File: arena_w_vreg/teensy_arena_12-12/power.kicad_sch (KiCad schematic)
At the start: 2 parts, among them J1 Barrel_Jack, SW1 SW_SPDT

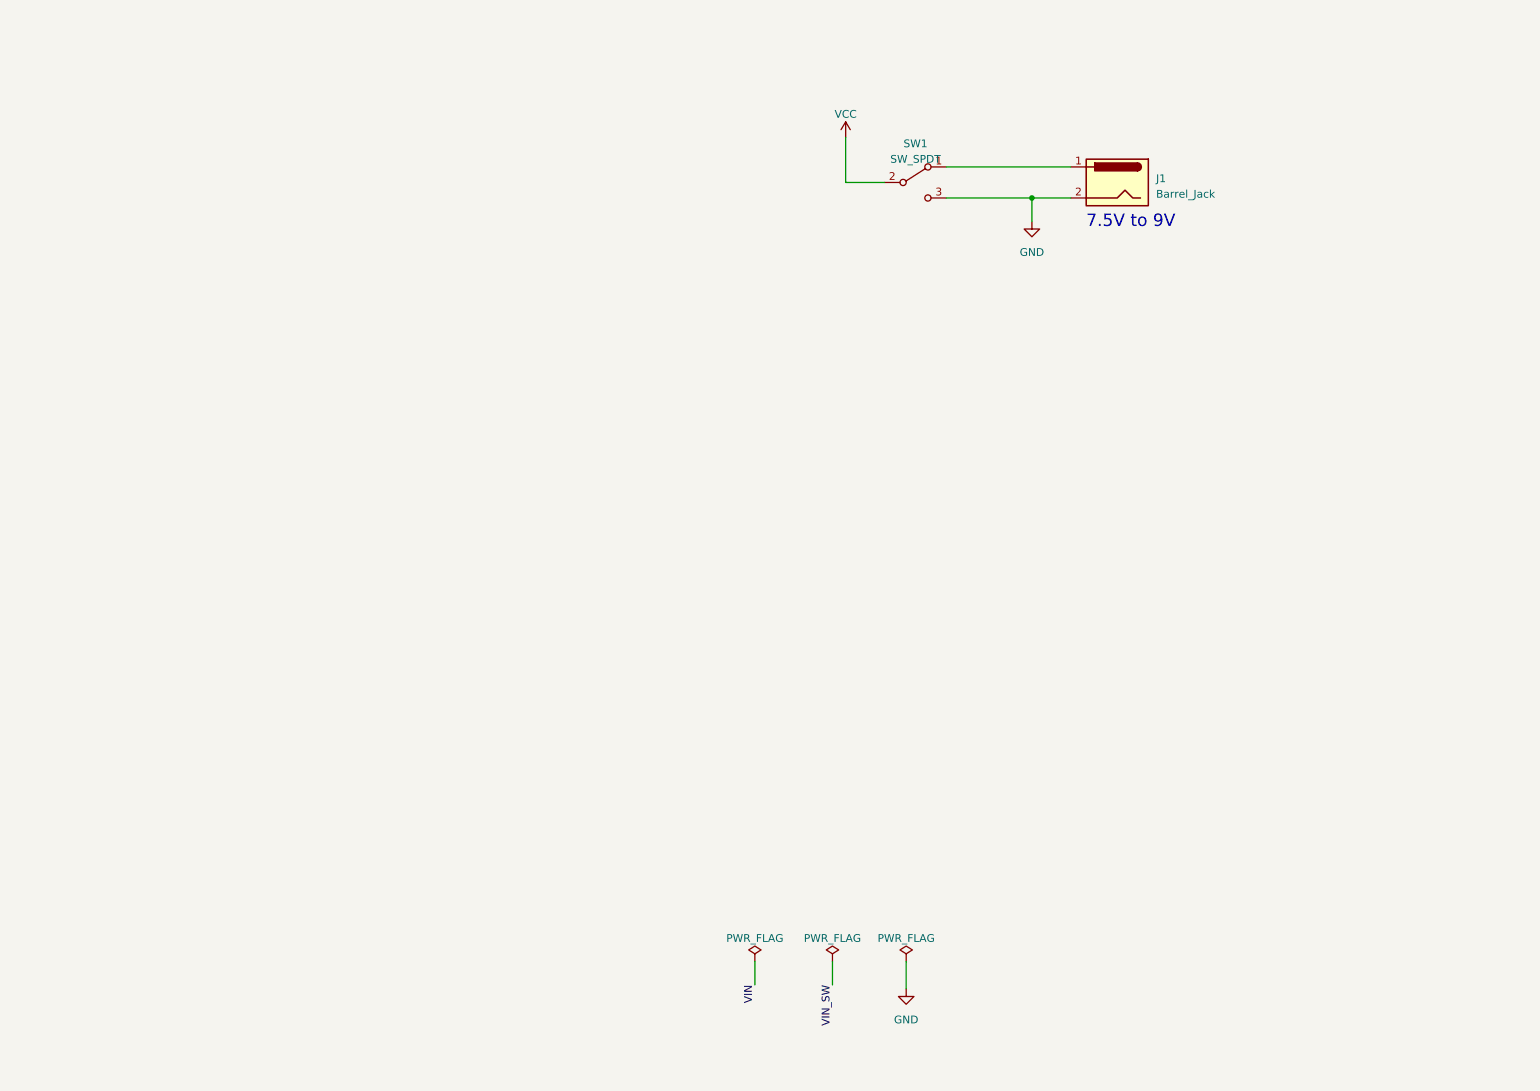
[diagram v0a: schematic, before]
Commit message: Completed initial schematic for 12-12 teensy arena.
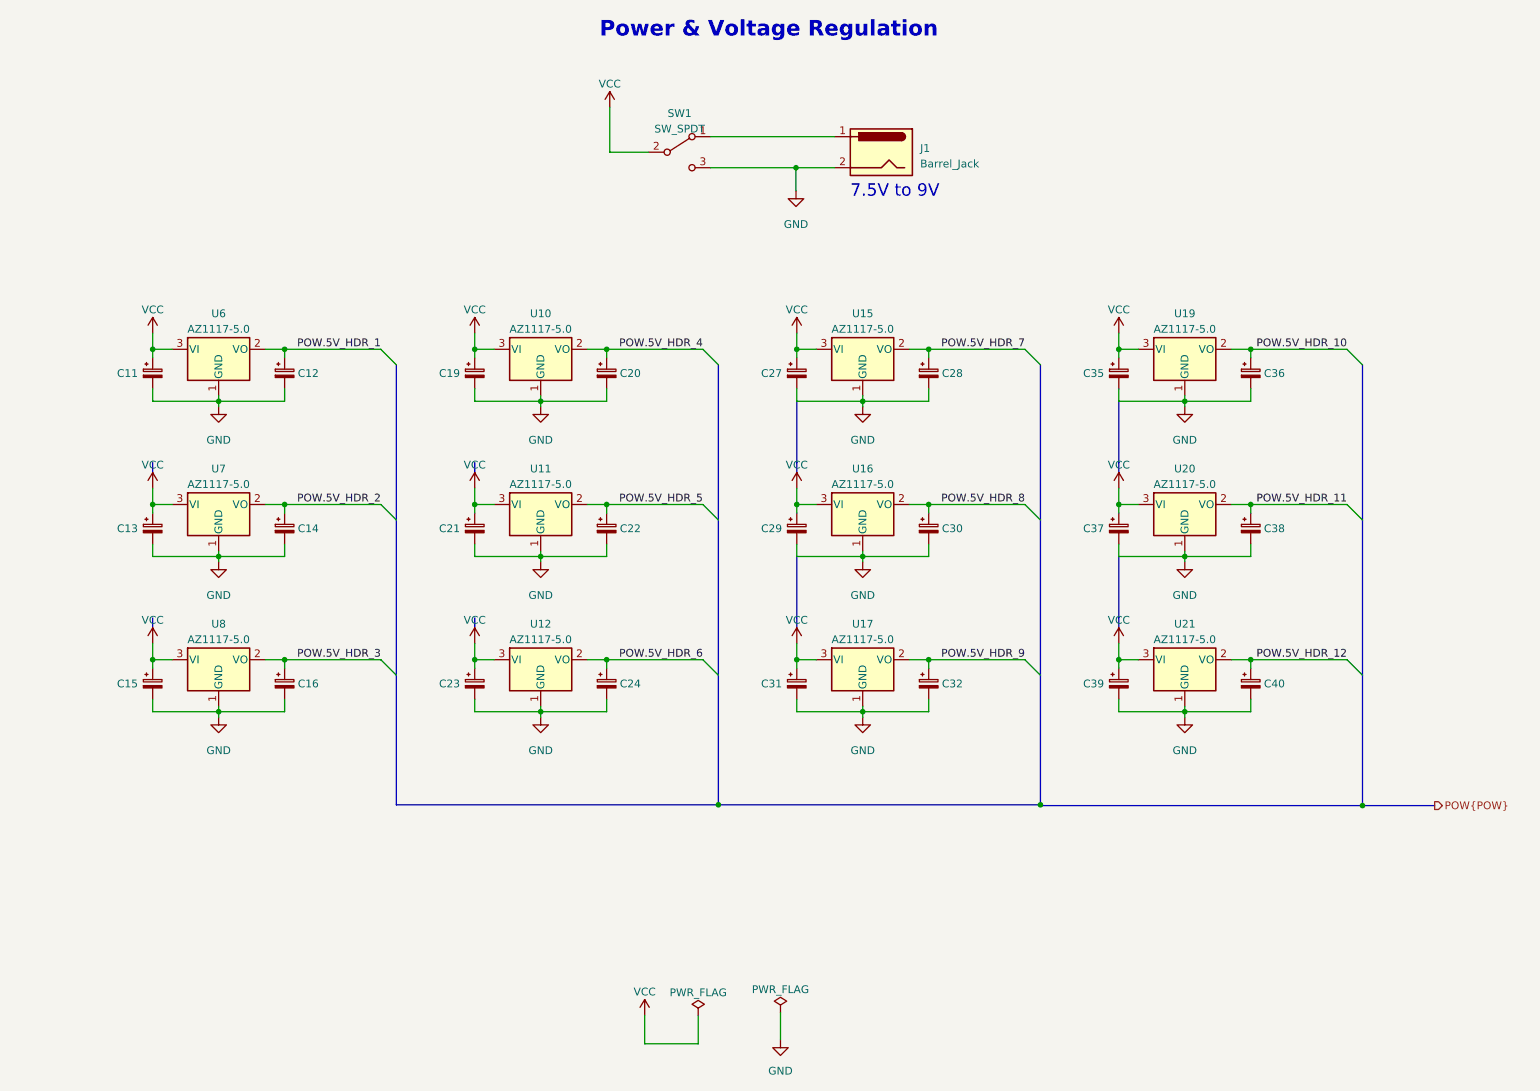
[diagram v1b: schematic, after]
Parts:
- added C11, C12, C13, C14, C15, C16, C19, C20, C21, C22, C23, C24, C27, C28, C29, C30, C31, C32, C35, C36, C37, C38, C39, C40: C_Polarized_Small, symbol Device:C_Polarized_Small
- added U10, U11, U12, U15, U16, U17, U19, U20, U21, U6, U7, U8: AZ1117-5.0, symbol Regulator_Linear:AZ1117-5.0
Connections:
- net GND: now also C11.2, C12.2, C13.2, C14.2, C15.2, C16.2, C19.2, C20.2, C21.2, C22.2, C23.2, C24.2, C27.2, C28.2, C29.2, C30.2, C31.2, C32.2, C35.2, C36.2, C37.2, C38.2, C39.2, C40.2, U10.1 (GND), U11.1 (GND), U12.1 (GND), U15.1 (GND), U16.1 (GND), U17.1 (GND), U19.1 (GND), U20.1 (GND), U21.1 (GND), U6.1 (GND), U7.1 (GND), U8.1 (GND)
- net VCC: now also C11.1, C13.1, C15.1, C19.1, C21.1, C23.1, C27.1, C29.1, C31.1, C35.1, C37.1, C39.1, U10.3 (VI), U11.3 (VI), U12.3 (VI), U15.3 (VI), U16.3 (VI), U17.3 (VI), U19.3 (VI), U20.3 (VI), U21.3 (VI), U6.3 (VI), U7.3 (VI), U8.3 (VI)
- new net POW.5V_HDR_1: C12.1, U6.2 (VO)
- new net POW.5V_HDR_10: C36.1, U19.2 (VO)
- new net POW.5V_HDR_11: C38.1, U20.2 (VO)
- new net POW.5V_HDR_12: C40.1, U21.2 (VO)
- new net POW.5V_HDR_2: C14.1, U7.2 (VO)
- new net POW.5V_HDR_3: C16.1, U8.2 (VO)
- new net POW.5V_HDR_4: C20.1, U10.2 (VO)
- new net POW.5V_HDR_5: C22.1, U11.2 (VO)
- new net POW.5V_HDR_6: C24.1, U12.2 (VO)
- new net POW.5V_HDR_7: C28.1, U15.2 (VO)
- new net POW.5V_HDR_8: C30.1, U16.2 (VO)
- new net POW.5V_HDR_9: C32.1, U17.2 (VO)
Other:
- note added: "Power & Voltage Regulation"
- moved on the sheet: J1, SW1

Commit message: Worked on 12-12 schematic & part selection.
Added new 5A regulators. Added load resistors so that regulators
always have minimum load.
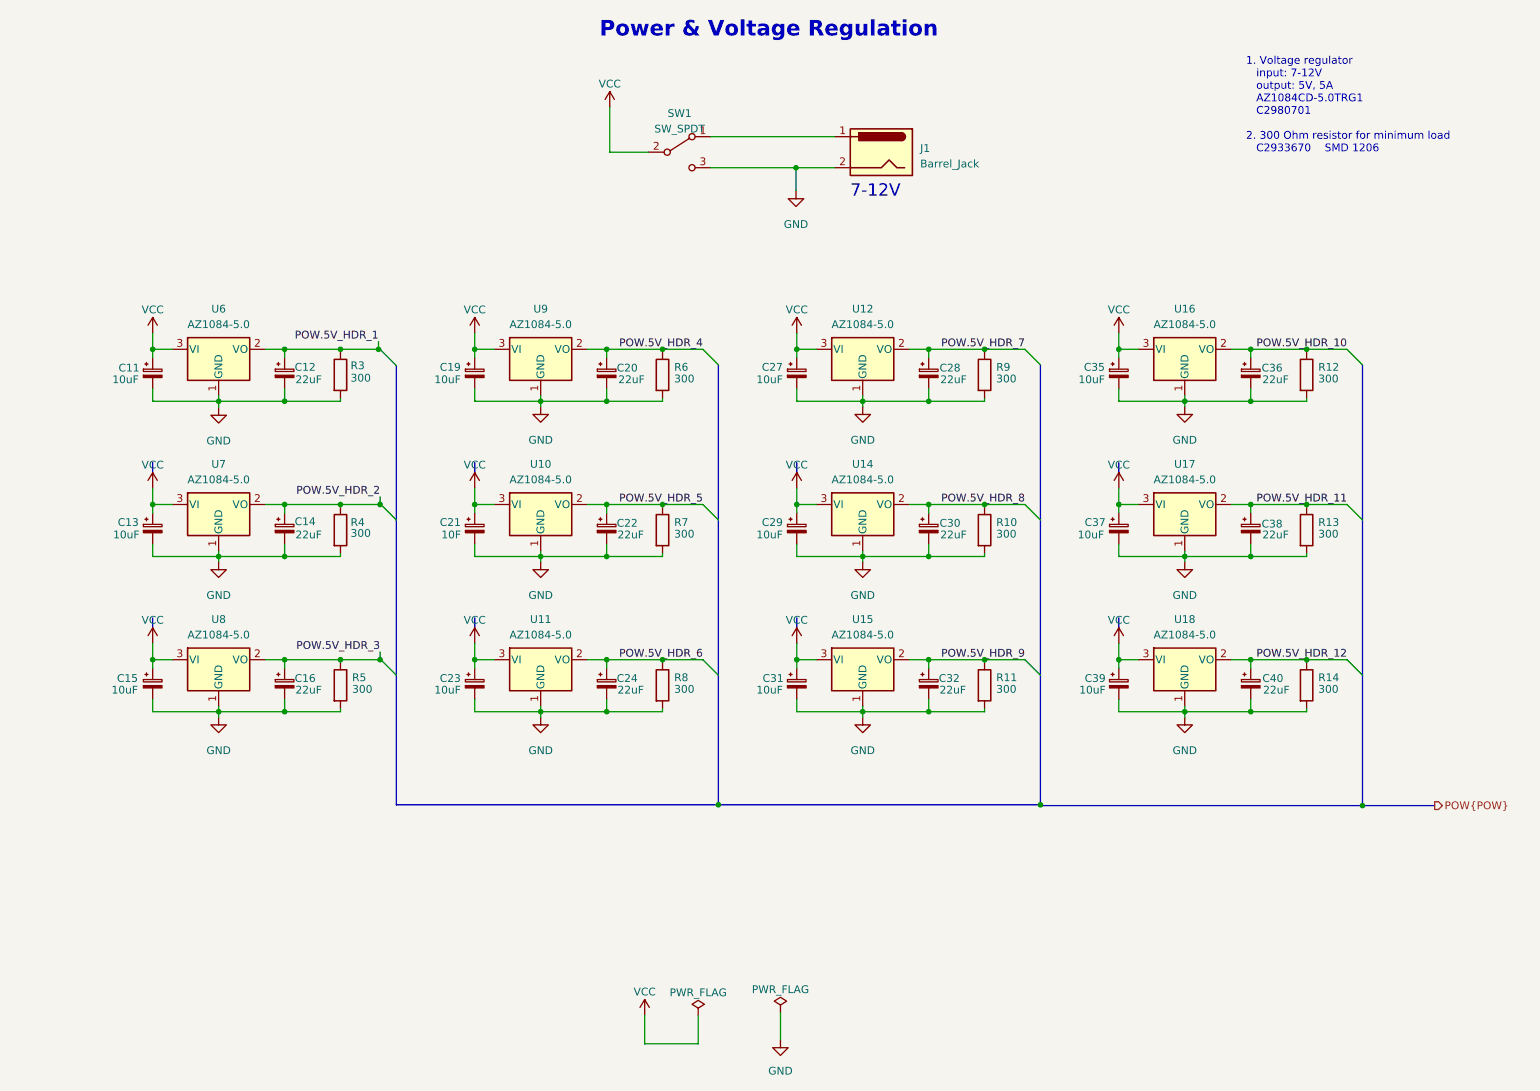
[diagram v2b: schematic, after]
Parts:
- removed U10, U11, U12, U15, U16, U17, U19, U20, U21, U6, U7, U8: AZ1117-5.0, symbol Regulator_Linear:AZ1117-5.0
- added R10, R11, R12, R13, R14, R3, R4, R5, R6, R7, R8, R9: 300, symbol Device:R
- added U10, U11, U12, U14, U15, U16, U17, U18, U6, U7, U8, U9: AZ1084-5.0, symbol Regulator_Linear:AZ1084-5.0
- C11, C13, C15, C19, C23, C27, C29, C31, C35, C37, C39: value C_Polarized_Small -> 10uF
- C12, C14, C16, C20, C22, C24, C28, C30, C32, C36, C38, C40: value C_Polarized_Small -> 22uF
- C21: value C_Polarized_Small -> 10F
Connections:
- net GND: now also R10.2, R11.2, R12.2, R13.2, R14.2, R3.2, R4.2, R5.2, R6.2, R7.2, R8.2, R9.2, U10.1 (GND), U11.1 (GND), U12.1 (GND), U14.1 (GND), U15.1 (GND), U16.1 (GND), U17.1 (GND), U18.1 (GND), U6.1 (GND), U7.1 (GND), U8.1 (GND), U9.1 (GND)
- net POW.5V_HDR_1: now also R3.1, U6.2 (VO)
- net POW.5V_HDR_10: now also R12.1, U16.2 (VO)
- net POW.5V_HDR_11: now also R13.1, U17.2 (VO)
- net POW.5V_HDR_12: now also R14.1, U18.2 (VO)
- net POW.5V_HDR_2: now also R4.1, U7.2 (VO)
- net POW.5V_HDR_3: now also R5.1, U8.2 (VO)
- net POW.5V_HDR_4: now also R6.1, U9.2 (VO)
- net POW.5V_HDR_5: now also R7.1, U10.2 (VO)
- net POW.5V_HDR_6: now also R8.1, U11.2 (VO)
- net POW.5V_HDR_7: now also R9.1, U12.2 (VO)
- net POW.5V_HDR_8: now also R10.1, U14.2 (VO)
- net POW.5V_HDR_9: now also R11.1, U15.2 (VO)
- net VCC: now also U10.3 (VI), U11.3 (VI), U12.3 (VI), U14.3 (VI), U15.3 (VI), U16.3 (VI), U17.3 (VI), U18.3 (VI), U6.3 (VI), U7.3 (VI), U8.3 (VI), U9.3 (VI)
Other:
- note added: "1. Voltage regulator input: 7-12V output: 5V, 5A AZ1084CD-5.0TRG1 C2980701 2. 300 Ohm resistor for minimum load C2933670 SMD 1206"
- note added: "7-12V"
- note removed: "7.5V to 9V"

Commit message: Finished footprint assignment. Added notes. Modified header footprint.
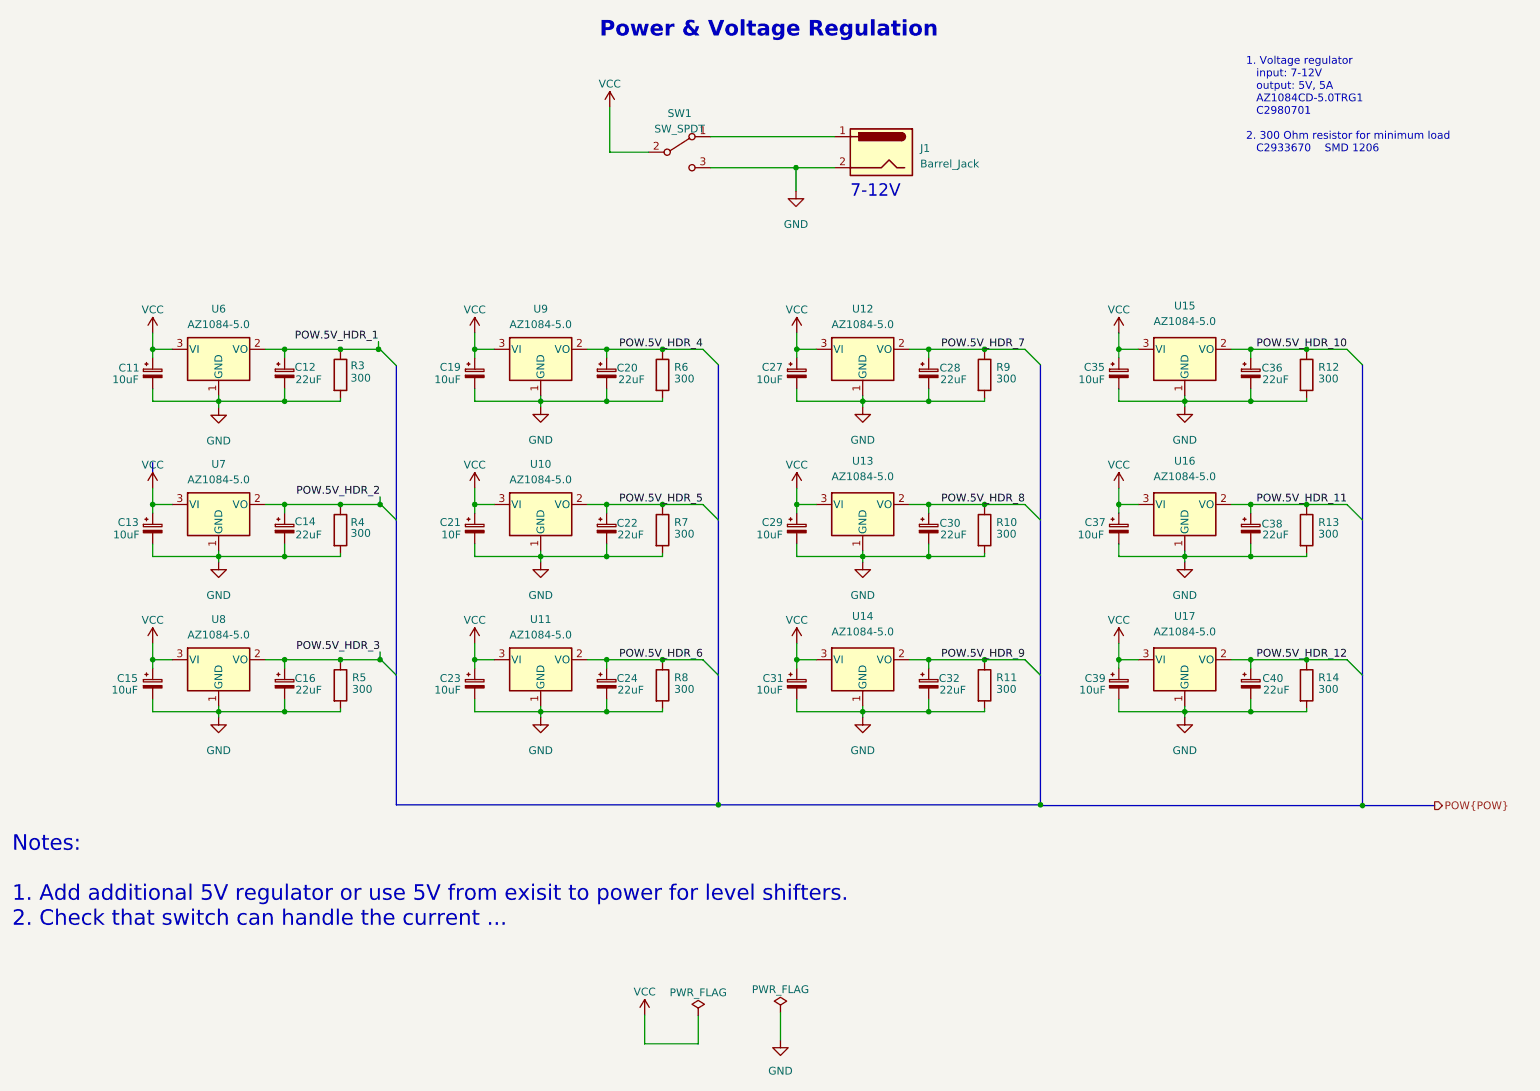
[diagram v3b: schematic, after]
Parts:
- C11, C12, C13, C14, C15, C16, C19, C20, C21, C22, C23, C24, C27, C28, C29, C30, C31, C32, C35, C36, C37, C38, C39, C40: footprint (none) -> Capacitor_SMD:CP_Elec_4x5.4
- R10, R11, R12, R13, R14, R3, R4, R5, R6, R7, R8, R9: footprint (none) -> Capacitor_SMD:C_1206_3216Metric
- U10, U11, U12, U6, U7, U8, U9: footprint (none) -> Package_TO_SOT_SMD:TO-252-3_TabPin2
- U13: renamed from U14; footprint (none) -> Package_TO_SOT_SMD:TO-252-3_TabPin2
- U14: renamed from U15; footprint (none) -> Package_TO_SOT_SMD:TO-252-3_TabPin2
- U15: renamed from U16; footprint (none) -> Package_TO_SOT_SMD:TO-252-3_TabPin2
- U16: renamed from U17; footprint (none) -> Package_TO_SOT_SMD:TO-252-3_TabPin2
- U17: renamed from U18; footprint (none) -> Package_TO_SOT_SMD:TO-252-3_TabPin2
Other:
- note added: "Notes: 1. Add additional 5V regulator or use 5V from exisit to power for level shifters. 2. Check that switch can handle the current ..."

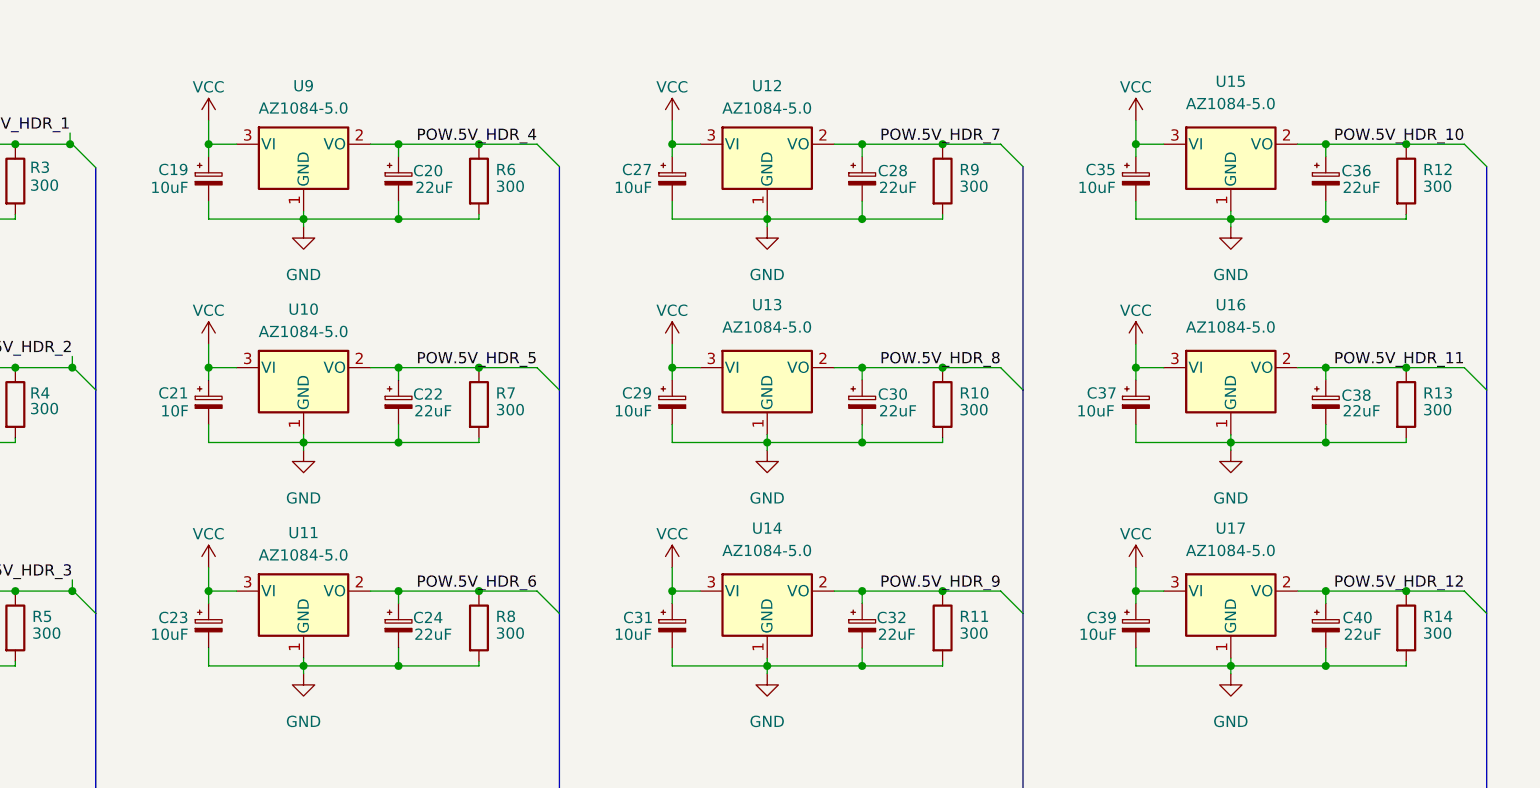
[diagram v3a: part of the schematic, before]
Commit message: Finished initial routing.
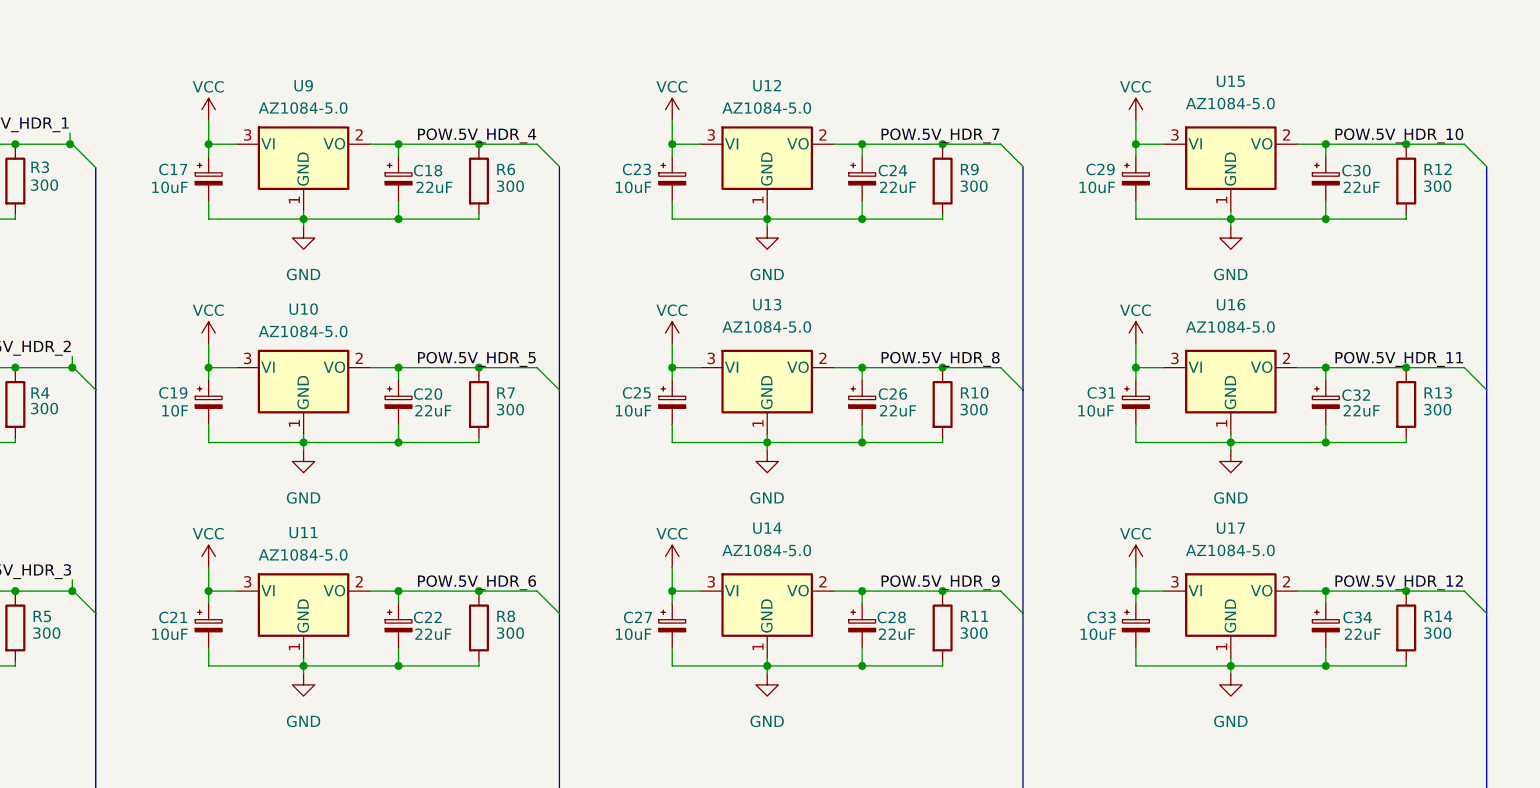
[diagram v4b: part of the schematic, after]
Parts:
- renumbered C19 to C17, C20 to C18, C21 to C19, C22 to C20, C23 to C21, C24 to C22, C27 to C23, C28 to C24, C29 to C25, C30 to C26, C31 to C27, C32 to C28, C35 to C29, C36 to C30, C37 to C31, C38 to C32, C39 to C33, C40 to C34
